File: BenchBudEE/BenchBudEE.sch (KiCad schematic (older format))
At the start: 0 parts

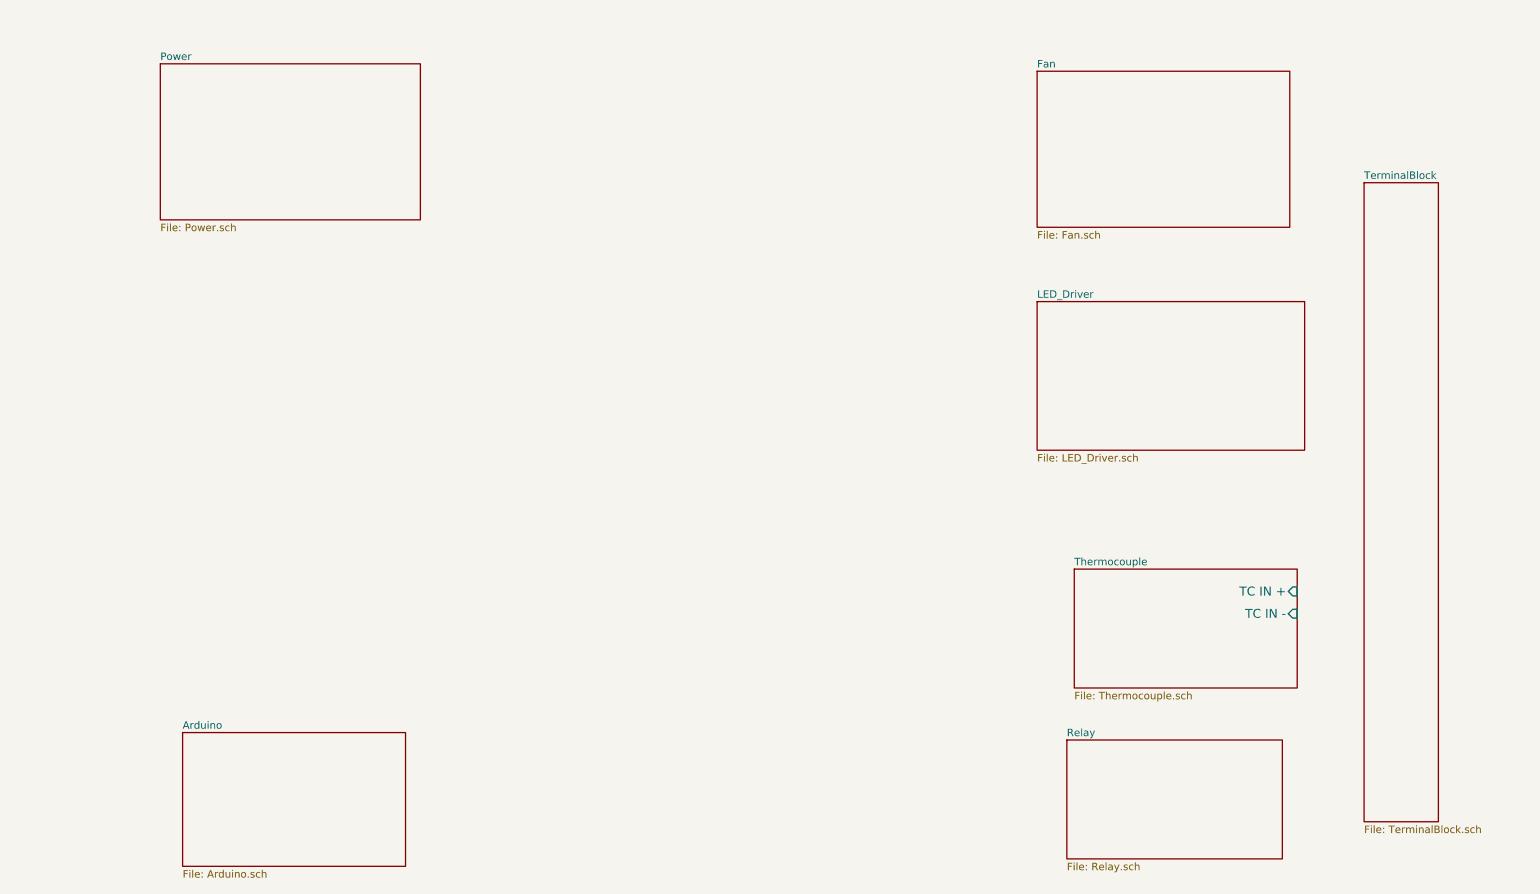
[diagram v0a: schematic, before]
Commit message: Defined block inputs and outputs.
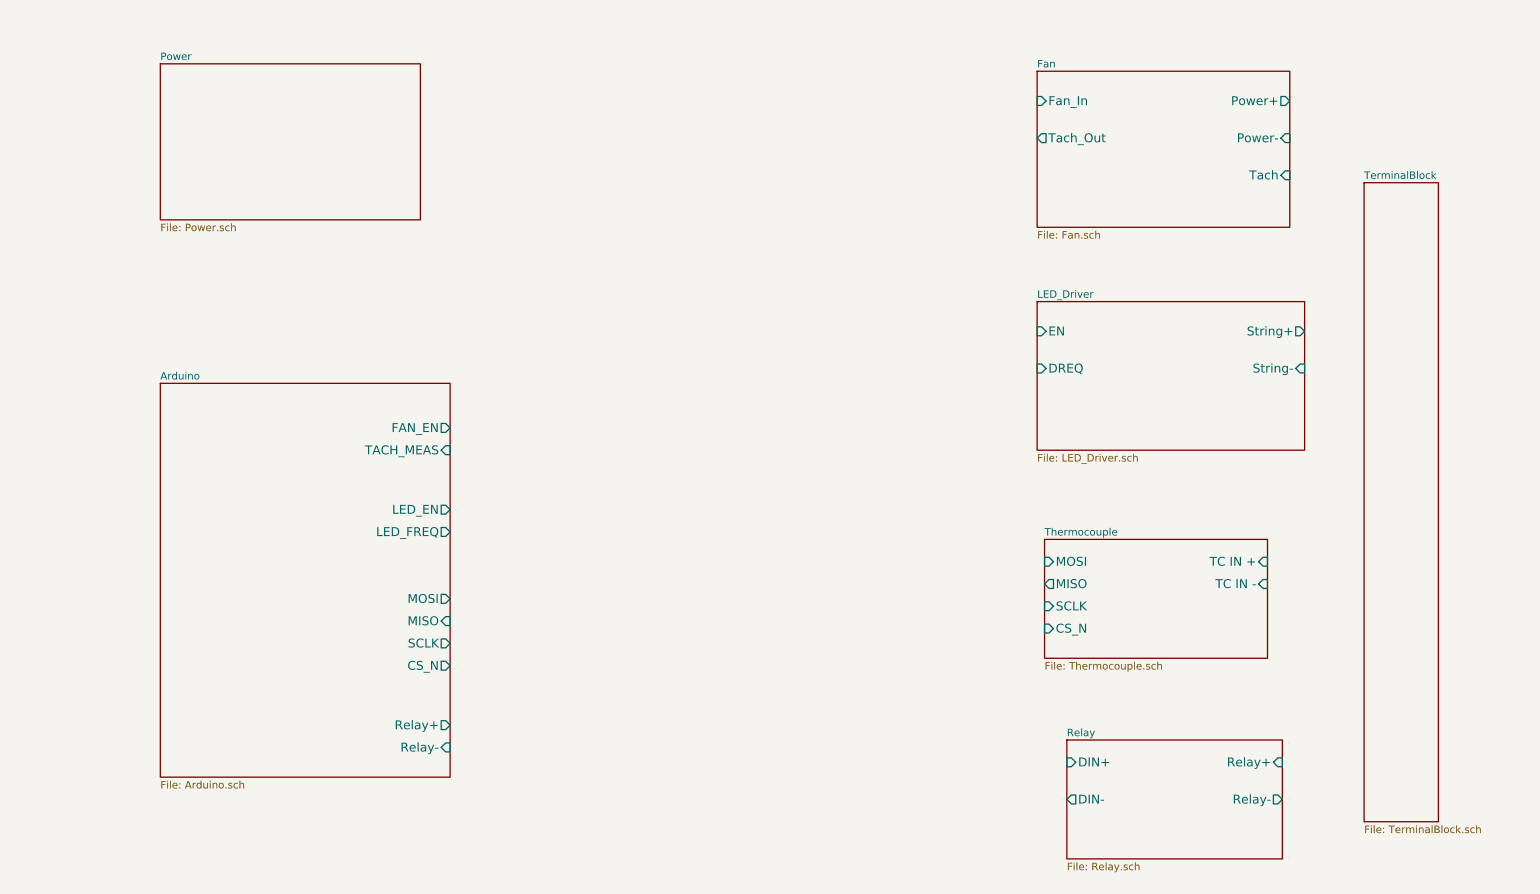
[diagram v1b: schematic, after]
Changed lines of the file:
@@
 $EndDescr
 $Sheet
-S 2100 5500 1500 900
+S 1950 3150 1950 2650
 U 52EC4D59
 F0 "Arduino" 50
 F1 "Arduino.sch" 50
+F2 "Relay+" O R 3900 5450 60
+F3 "Relay-" I R 3900 5600 60
+F4 "MOSI" O R 3900 4600 60
+F5 "MISO" I R 3900 4750 60
+F6 "SCLK" O R 3900 4900 60
+F7 "CS_N" O R 3900 5050 60
+F8 "LED_EN" O R 3900 4000 60
+F9 "LED_FREQ" O R 3900 4150 60
+F10 "FAN_EN" O R 3900 3450 60
+F11 "TACH_MEAS" I R 3900 3600 60
 $EndSheet
 $Sheet
-S 8100 4400 1500 800
+S 7900 4200 1500 800
 U 52EC4DA4
 F0 "Thermocouple" 50
 F1 "Thermocouple.sch" 50
-F2 "TC IN +" I R 9600 4550 60
-F3 "TC IN -" I R 9600 4700 60
+F2 "TC IN +" I R 9400 4350 60
+F3 "TC IN -" I R 9400 4500 60
+F4 "MOSI" I L 7900 4350 60
+F5 "MISO" O L 7900 4500 60
+F6 "SCLK" I L 7900 4650 60
+F7 "CS_N" I L 7900 4800 60
 $EndSheet
 $Sheet
@@
 F0 "Relay" 50
 F1 "Relay.sch" 50
+F2 "DIN+" I L 8050 5700 60
+F3 "DIN-" O L 8050 5950 60
+F4 "Relay+" I R 9500 5700 60
+F5 "Relay-" O R 9500 5950 60
 $EndSheet
 $Sheet
@@
 F0 "LED_Driver" 50
 F1 "LED_Driver.sch" 50
+F2 "EN" I L 7850 2800 60
+F3 "DREQ" I L 7850 3050 60
+F4 "String+" O R 9650 2800 60
+F5 "String-" I R 9650 3050 60
 $EndSheet
 $Sheet
@@
 F0 "Fan" 50
 F1 "Fan.sch" 50
+F2 "Power+" O R 9550 1250 60
+F3 "Power-" I R 9550 1500 60
+F4 "Tach" I R 9550 1750 60
+F5 "Tach_Out" O L 7850 1500 60
+F6 "Fan_In" I L 7850 1250 60
 $EndSheet
 $Sheet

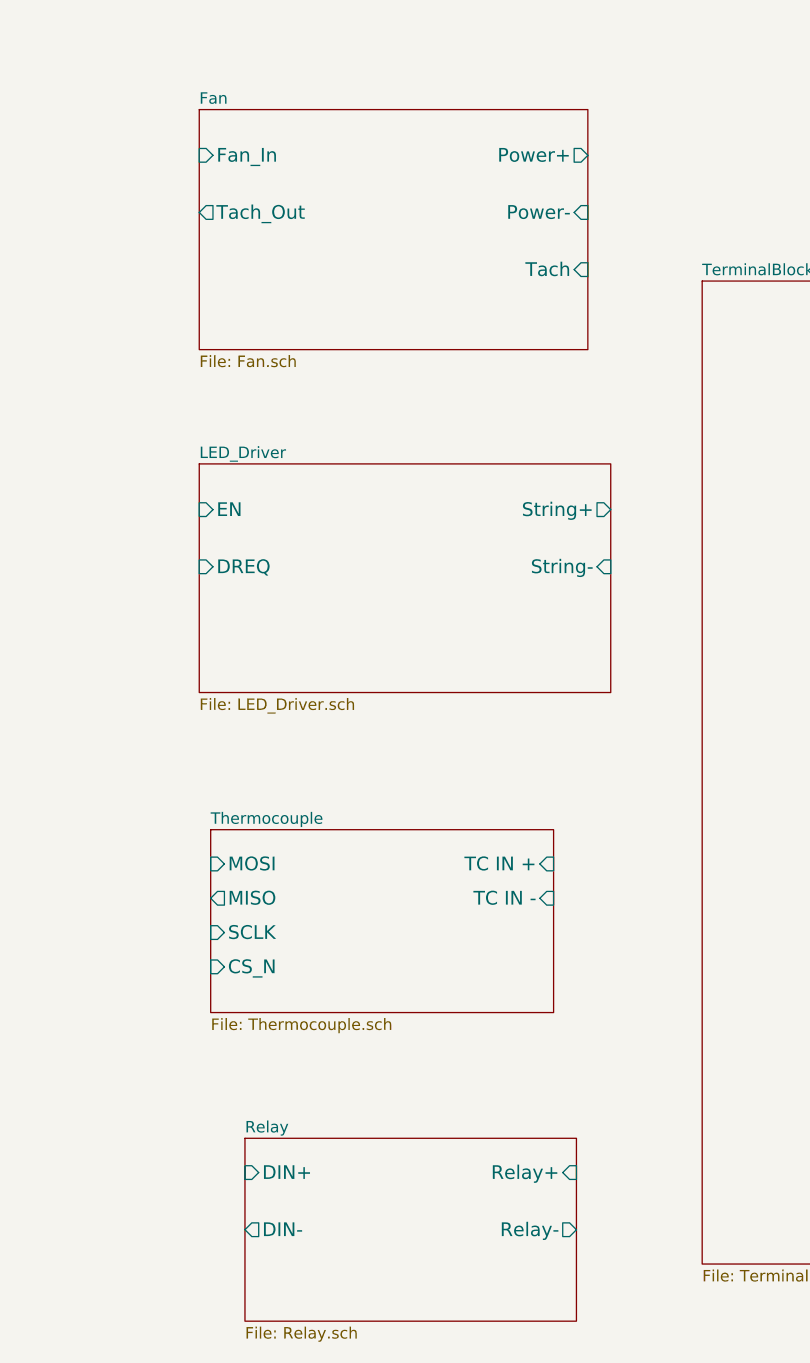
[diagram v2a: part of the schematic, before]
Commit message: Roughly filled in the Fan sheet.
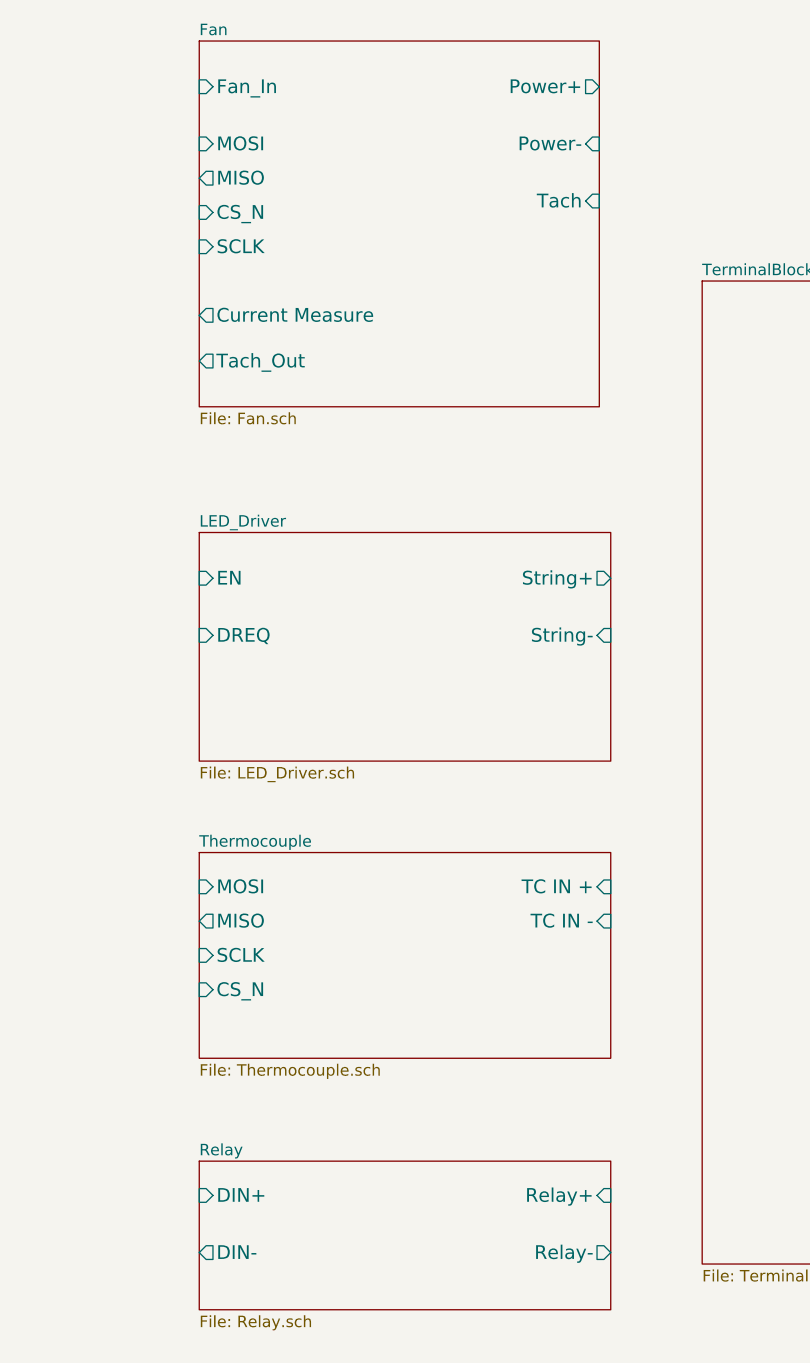
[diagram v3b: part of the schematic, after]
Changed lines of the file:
@@
 Sheet 1 8
 Title ""
-Date "5 feb 2014"
+Date "6 feb 2014"
 Rev ""
 Comp ""
@@
 $EndSheet
 $Sheet
-S 7900 4200 1500 800
+S 7850 4300 1800 900
 U 52EC4DA4
 F0 "Thermocouple" 50
 F1 "Thermocouple.sch" 50
-F2 "TC IN +" I R 9400 4350 60
-F3 "TC IN -" I R 9400 4500 60
-F4 "MOSI" I L 7900 4350 60
-F5 "MISO" O L 7900 4500 60
-F6 "SCLK" I L 7900 4650 60
-F7 "CS_N" I L 7900 4800 60
+F2 "TC IN +" I R 9650 4450 60
+F3 "TC IN -" I R 9650 4600 60
+F4 "MOSI" I L 7850 4450 60
+F5 "MISO" O L 7850 4600 60
+F6 "SCLK" I L 7850 4750 60
+F7 "CS_N" I L 7850 4900 60
 $EndSheet
 $Sheet
-S 8050 5550 1450 800
+S 7850 5650 1800 650
 U 52EC4DB9
 F0 "Relay" 50
 F1 "Relay.sch" 50
-F2 "DIN+" I L 8050 5700 60
-F3 "DIN-" O L 8050 5950 60
-F4 "Relay+" I R 9500 5700 60
-F5 "Relay-" O R 9500 5950 60
+F2 "DIN+" I L 7850 5800 60
+F3 "DIN-" O L 7850 6050 60
+F4 "Relay+" I R 9650 5800 60
+F5 "Relay-" O R 9650 6050 60
 $EndSheet
 $Sheet
@@
 $EndSheet
 $Sheet
-S 7850 2600 1800 1000
+S 7850 2900 1800 1000
 U 52EC4DEA
 F0 "LED_Driver" 50
 F1 "LED_Driver.sch" 50
-F2 "EN" I L 7850 2800 60
-F3 "DREQ" I L 7850 3050 60
-F4 "String+" O R 9650 2800 60
-F5 "String-" I R 9650 3050 60
+F2 "EN" I L 7850 3100 60
+F3 "DREQ" I L 7850 3350 60
+F4 "String+" O R 9650 3100 60
+F5 "String-" I R 9650 3350 60
 $EndSheet
 $Sheet
-S 7850 1050 1700 1050
+S 7850 750  1750 1600
 U 52EC4E13
 F0 "Fan" 50
 F1 "Fan.sch" 50
-F2 "Power+" O R 9550 1250 60
-F3 "Power-" I R 9550 1500 60
-F4 "Tach" I R 9550 1750 60
-F5 "Tach_Out" O L 7850 1500 60
-F6 "Fan_In" I L 7850 1250 60
+F2 "Power+" O R 9600 950 60
+F3 "Power-" I R 9600 1200 60
+F4 "Tach" I R 9600 1450 60
+F5 "Tach_Out" O L 7850 2150 60
+F6 "Fan_In" I L 7850 950 60
+F7 "Current Measure" O L 7850 1950 60
+F8 "MOSI" I L 7850 1200 60
+F9 "MISO" O L 7850 1350 60
+F10 "CS_N" I L 7850 1500 60
+F11 "SCLK" I L 7850 1650 60
 $EndSheet
 $Sheet

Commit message: Roughly populated the Power sheet.
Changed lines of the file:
@@
 $Descr A4 11693 8268
 encoding utf-8
-Sheet 1 8
+Sheet 1 9
 Title ""
-Date "7 feb 2014"
+Date "8 feb 2014"
 Rev ""
 Comp ""
@@
 F1 "TerminalBlock.sch" 50
 $EndSheet
+$Sheet
+S 4700 1000 1700 1050
+U 52F627C8
+F0 "PowerAdjustmentMonitor" 50
+F1 "PowerAdjustmentMonitor.sch" 50
+$EndSheet
 $EndSCHEMATC

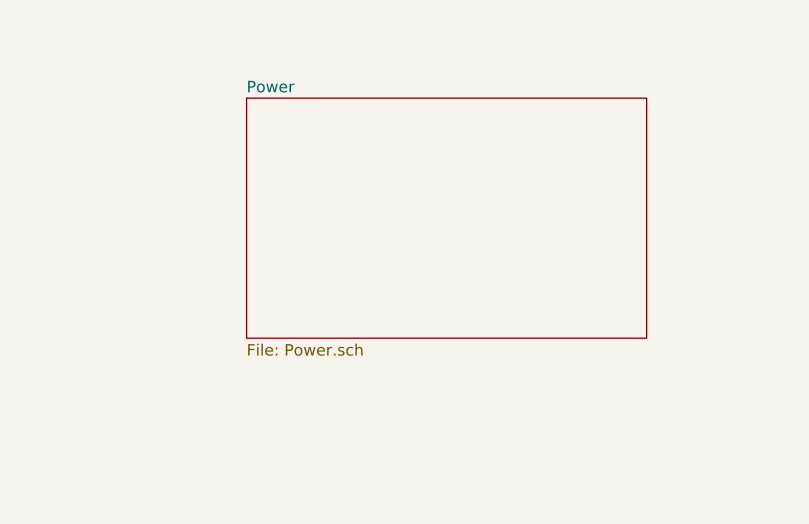
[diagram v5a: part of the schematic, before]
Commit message: Populated the Power Adjustment Monitor sheet in rough form.
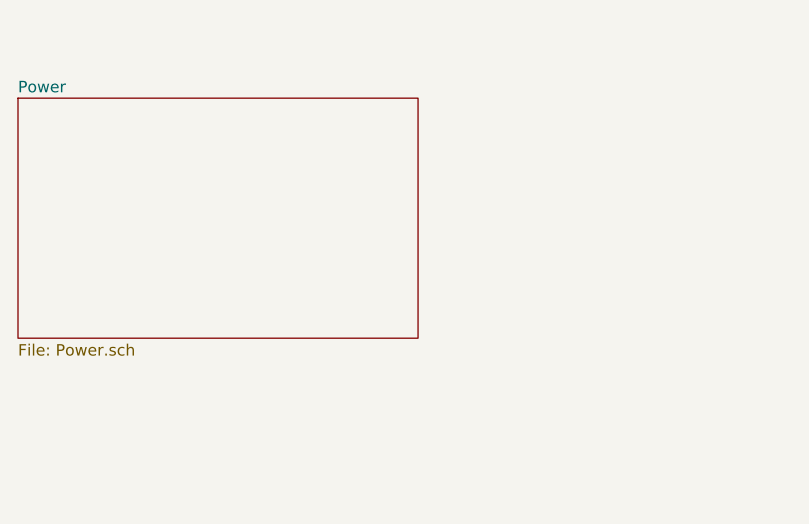
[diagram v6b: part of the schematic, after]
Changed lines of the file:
@@
 Sheet 1 9
 Title ""
-Date "8 feb 2014"
+Date "9 feb 2014"
 Rev ""
 Comp ""
@@
 $EndSheet
 $Sheet
-S 1950 1000 1750 1050
+S 950  1000 1750 1050
 U 52EC4DDC
 F0 "Power" 50
